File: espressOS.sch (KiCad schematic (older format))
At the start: 22 parts

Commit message: Add temperature sensors
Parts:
- added J?: LMT01_CONN1, symbol Connector_Generic:Conn_01x02
- added J?: LMT01_WIRE1, symbol Connector_Generic:Conn_01x02
- added J?: LMT01_CONN2, symbol Connector_Generic:Conn_01x02
- added J?: LMT01_WIRE2, symbol Connector_Generic:Conn_01x02
- added J?: LMT01_CONN3, symbol Connector_Generic:Conn_01x02
- added J?: LMT01_WIRE3, symbol Connector_Generic:Conn_01x02
- added Q?: 2N3904, Package_TO_SOT_THT:TO-92_Inline, symbol Transistor_BJT:2N3904
- added R?: 10k, symbol Device:R_US
- added U? (x3): LMT01, symbol espressOS:LMT01
- SW?: value SW_Push -> SPST
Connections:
- net labels added: LMT01_1_CTRL, LMT01_2_CTRL, LMT01_3_CTRL, LMT01_OUT
- wire segments 106 -> 130
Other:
- moved on the sheet: C?, R?, SW?, Y?

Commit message: Add LMT01 control pins
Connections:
- wire segments 130 -> 133
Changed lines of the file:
@@
 Text Label 6250 3100 0    50   ~ 0
 SWD_IO
+Wire Wire Line
+	5950 3000 6250 3000
+Text Label 6250 3000 0    50   ~ 0
+LMT01_1_CTRL
+Wire Wire Line
+	5950 4300 6250 4300
+Wire Wire Line
+	5950 4400 6250 4400
+Text Label 6250 4300 0    50   ~ 0
+LMT01_2_CTRL
+Text Label 6250 4400 0    50   ~ 0
+LMT01_3_CTRL
 $EndSCHEMATC

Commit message: Update board
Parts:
- removed J?: FTSH-105-01-L-DV-K, SAMTEC_FTSH-105-01-L-DV-K, symbol FTSH-105-01-L-DV-K:FTSH-105-01-L-DV-K
- added J?: FTSH-105-01-L-DV-K, SAMTEC_FTSH-105-01-L-DV-K, symbol espressOS:FTSH-105-01-L-DV-K
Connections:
- net labels added: AC
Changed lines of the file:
@@
 EESchema Schematic File Version 4
-LIBS:espressOS-cache
 EELAYER 30 0
 EELAYER END
@@
 $EndDescr
 $Comp
-L FTSH-105-01-L-DV-K:FTSH-105-01-L-DV-K J?
-U 1 1 5E4E12B7
-P 5150 6600
-F 0 "J?" H 5150 7070 50  0000 C CNN
-F 1 "FTSH-105-01-L-DV-K" H 5150 6979 50  0000 C CNN
-F 2 "SAMTEC_FTSH-105-01-L-DV-K" H 4950 5750 50  0001 L BNN
-F 3 "FTSH-105-01-L-DV-K-TR" H 4950 5850 50  0001 L BNN
-	1    5150 6600
-	1    0    0    -1
-$EndComp
-$Comp
 L power:VDD #PWR?
 U 1 1 5E4E253E
-P 4300 6350
-F 0 "#PWR?" H 4300 6200 50  0001 C CNN
-F 1 "VDD" H 4317 6523 50  0000 C CNN
-F 2 "" H 4300 6350 50  0001 C CNN
-F 3 "" H 4300 6350 50  0001 C CNN
-	1    4300 6350
-	1    0    0    -1
-$EndComp
-Wire Wire Line
-	4300 6350 4300 6500
-Wire Wire Line
-	4300 6500 4450 6500
+P 5000 6350
+F 0 "#PWR?" H 5000 6200 50  0001 C CNN
+F 1 "VDD" H 5017 6523 50  0000 C CNN
+F 2 "" H 5000 6350 50  0001 C CNN
+F 3 "" H 5000 6350 50  0001 C CNN
+	1    5000 6350
+	1    0    0    -1
+$EndComp
+Wire Wire Line
+	5000 6350 5000 6500
+Wire Wire Line
+	5000 6500 5150 6500
 $Comp
 L power:GND #PWR?
 U 1 1 5E4E2DCF
-P 4300 7150
-F 0 "#PWR?" H 4300 6900 50  0001 C CNN
-F 1 "GND" H 4305 6977 50  0000 C CNN
-F 2 "" H 4300 7150 50  0001 C CNN
-F 3 "" H 4300 7150 50  0001 C CNN
-	1    4300 7150
-	1    0    0    -1
-$EndComp
-Wire Wire Line
-	4300 7150 4300 6900
-Wire Wire Line
-	4300 6600 4450 6600
-Wire Wire Line
-	4450 6700 4300 6700
-Connection ~ 4300 6700
-Wire Wire Line
-	4300 6700 4300 6600
-Wire Wire Line
-	4450 6900 4300 6900
-Connection ~ 4300 6900
-Wire Wire Line
-	4300 6900 4300 6700
+P 5000 7150
+F 0 "#PWR?" H 5000 6900 50  0001 C CNN
+F 1 "GND" H 5005 6977 50  0000 C CNN
+F 2 "" H 5000 7150 50  0001 C CNN
+F 3 "" H 5000 7150 50  0001 C CNN
+	1    5000 7150
+	1    0    0    -1
+$EndComp
+Wire Wire Line
+	5000 7150 5000 6900
+Wire Wire Line
+	5000 6600 5150 6600
+Wire Wire Line
+	5150 6700 5000 6700
+Connection ~ 5000 6700
+Wire Wire Line
+	5000 6700 5000 6600
+Wire Wire Line
+	5150 6900 5000 6900
+Connection ~ 5000 6900
+Wire Wire Line
+	5000 6900 5000 6700
 Wire Wire Line
 	5850 6500 6050 6500
@@
 Text Label 6250 4400 0    50   ~ 0
 LMT01_3_CTRL
+$Comp
+L power:AC #PWR?
+U 1 1 5E40F9F2
+P 1550 1300
+F 0 "#PWR?" H 1550 1200 50  0001 C CNN
+F 1 "AC" H 1550 1575 50  0000 C CNN
+F 2 "" H 1550 1300 50  0001 C CNN
+F 3 "" H 1550 1300 50  0001 C CNN
+	1    1550 1300
+	1    0    0    -1
+$EndComp
+$Comp
+L espressOS:FTSH-105-01-L-DV-K J?
+U 1 1 5E637338
+P 5500 6600
+F 0 "J?" H 5500 6970 50  0000 C CNN
+F 1 "FTSH-105-01-L-DV-K" H 5500 6879 50  0000 C CNN
+F 2 "SAMTEC_FTSH-105-01-L-DV-K" H 5350 5900 50  0001 L BNN
+F 3 "FTSH-105-01-L-DV-K-TR" H 5350 6000 50  0001 L BNN
+	1    5500 6600
+	1    0    0    -1
+$EndComp
 $EndSCHEMATC

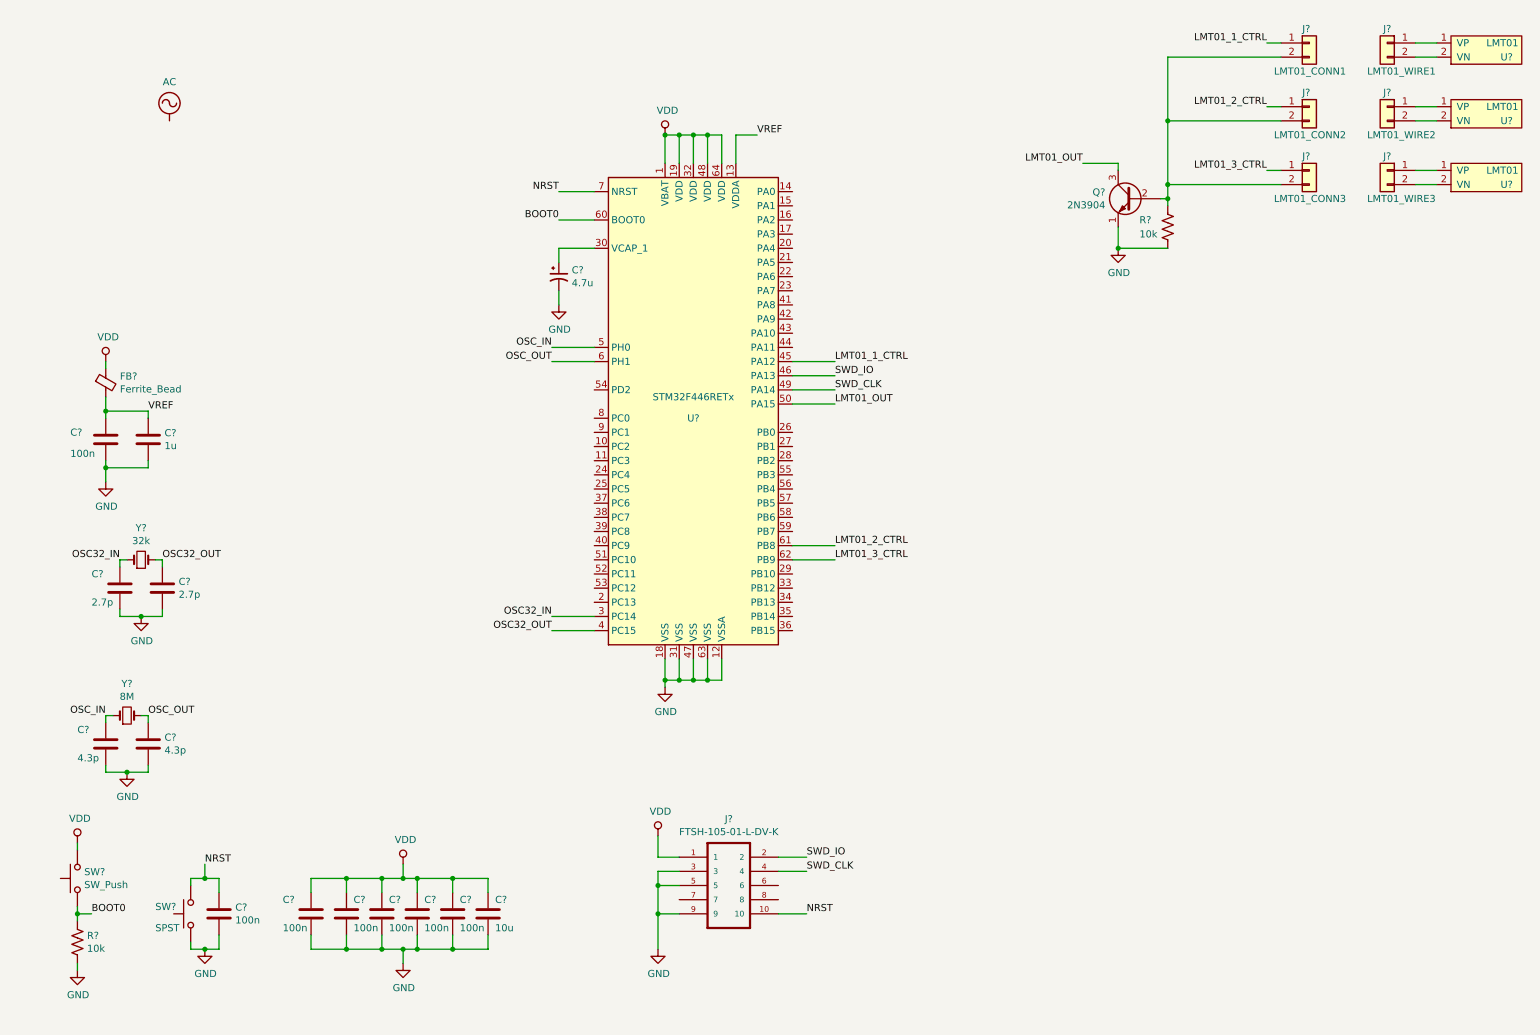
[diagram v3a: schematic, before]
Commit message: Add many components and signals
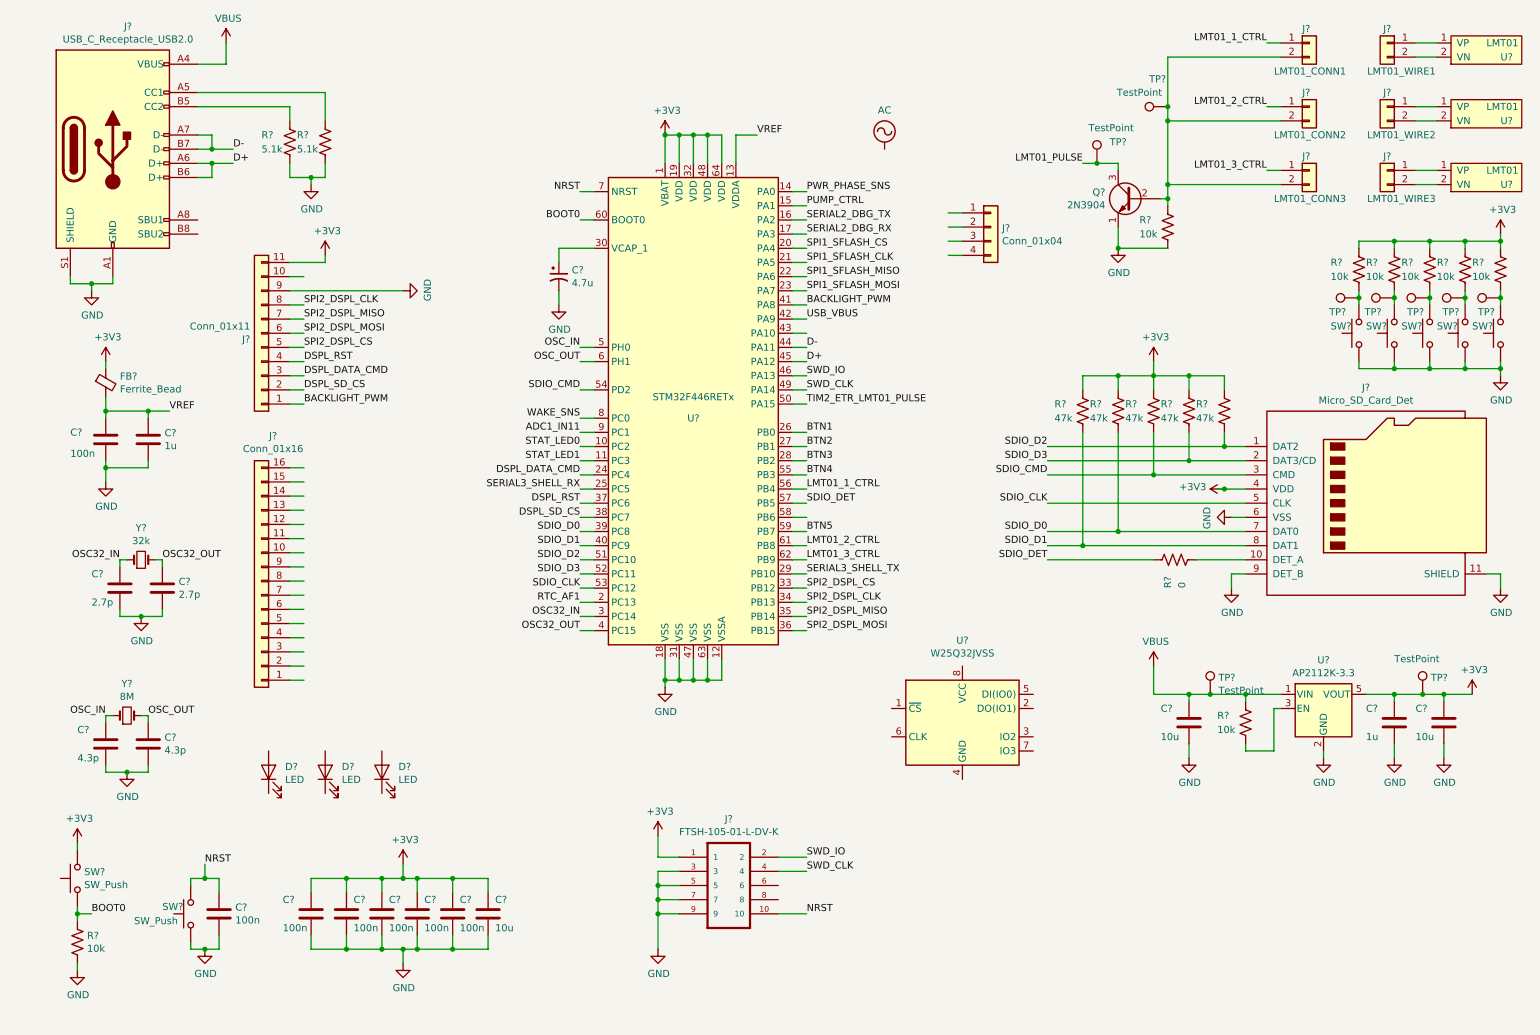
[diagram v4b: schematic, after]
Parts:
- removed SW?: SPST, symbol Switch:SW_Push
- added C?: 1u, symbol Device:C
- added C? (x2): 10u, symbol Device:C
- added D? (x3): LED, symbol Device:LED
- added J?: Micro_SD_Card_Det, symbol Connector:Micro_SD_Card_Det
- added J?: USB_C_Receptacle_USB2.0, symbol Connector:USB_C_Receptacle_USB2.0
- added J?: Conn_01x11, symbol Connector_Generic:Conn_01x11
- added J?: Conn_01x04, symbol Connector_Generic:Conn_01x04
- added J?: Conn_01x16, symbol Connector_Generic:Conn_01x16
- added R? (x2): 5.1k, symbol Device:R_US
- added R? (x5): 47k, symbol Device:R_US
- added R? (x6): 10k, symbol Device:R_US
- added R?: 0, symbol Device:R_US
- added SW? (x6): SW_Push, symbol Switch:SW_Push
- added TP? (x9): TestPoint, symbol Connector:TestPoint
- added U?: W25Q32JVSS, Package_SO:SOIC-8_5.23x5.23mm_P1.27mm, symbol Memory_Flash:W25Q32JVSS
- added U?: AP2112K-3.3, Package_TO_SOT_SMD:SOT-23-5, symbol Regulator_Linear:AP2112K-3.3
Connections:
- net labels added: +3V3, ADC1_IN11, BACKLIGHT_PWM, BTN1, BTN2, BTN3, BTN4, BTN5, D+, D-, DSPL_DATA_CMD, DSPL_RST, DSPL_SD_CS, LMT01_PULSE, PUMP_CTRL, PWR_PHASE_SNS, RTC_AF1, SDIO_CLK, SDIO_CMD, SDIO_D0, SDIO_D1, SDIO_D2, SDIO_D3, SDIO_DET, SERIAL2_DBG_RX, SERIAL2_DBG_TX, SERIAL3_SHELL_RX, SERIAL3_SHELL_TX, SPI1_SFLASH_CLK, SPI1_SFLASH_CS, SPI1_SFLASH_MISO, SPI1_SFLASH_MOSI, SPI2_DSPL_CLK, SPI2_DSPL_CS, SPI2_DSPL_MISO, SPI2_DSPL_MOSI, STAT_LED0, STAT_LED1, TIM2_ETR_LMT01_PULSE, USB_VBUS, VBUS, WAKE_SNS
- net labels removed: LMT01_OUT, VDD
- wire segments 133 -> 320

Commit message: Add lots more wiring
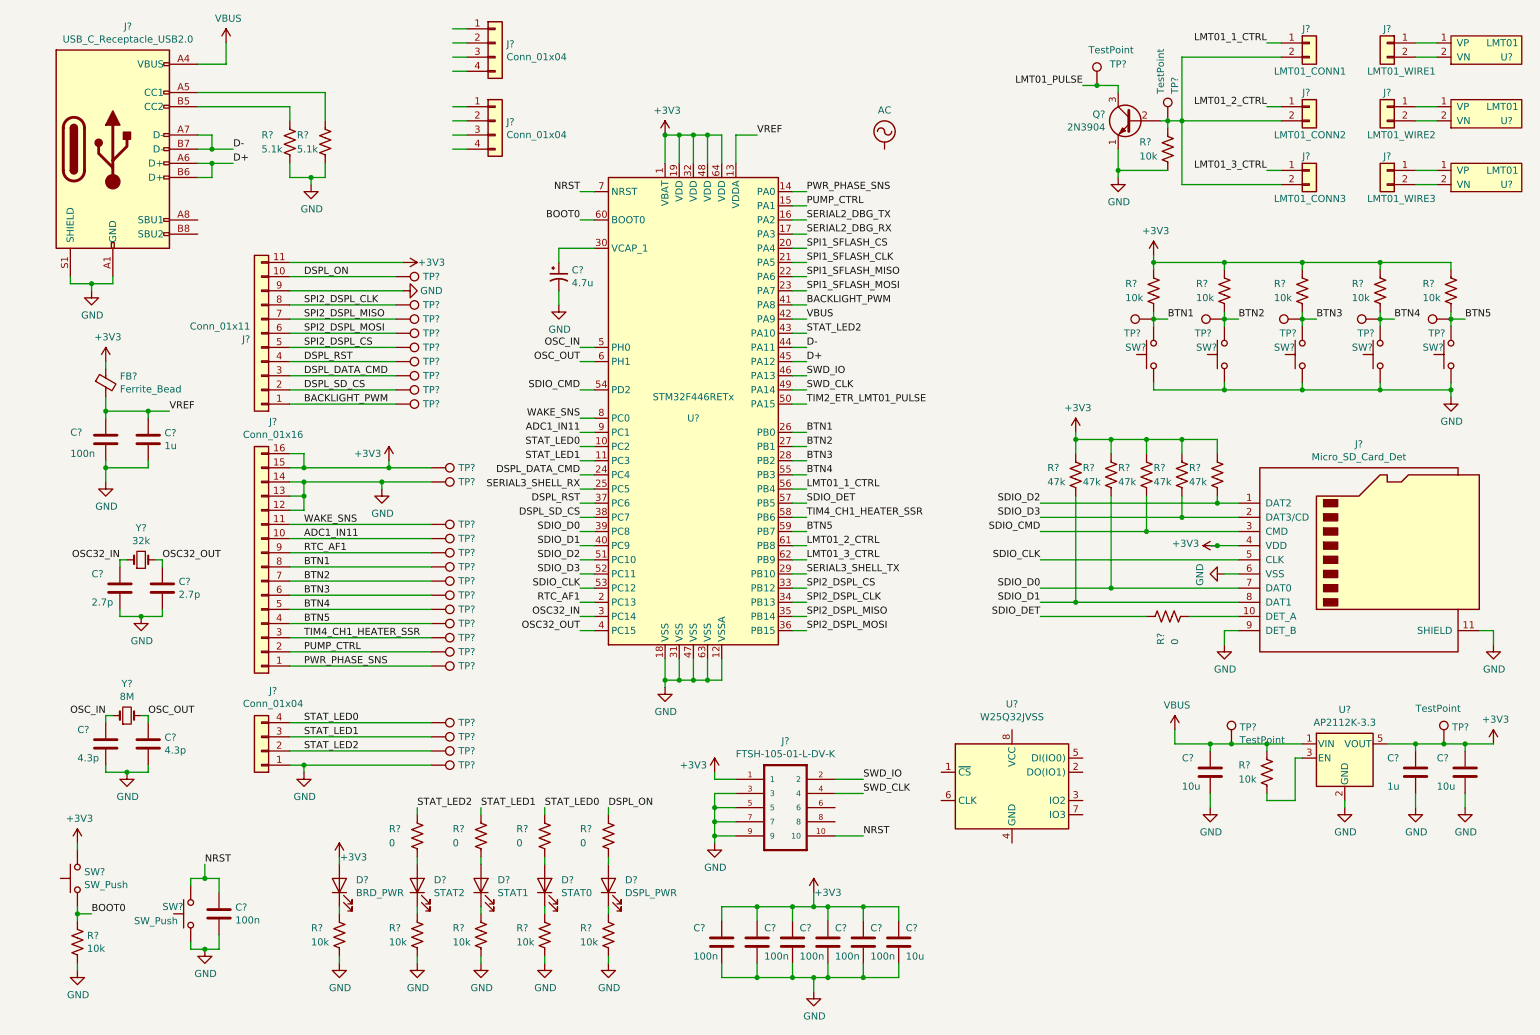
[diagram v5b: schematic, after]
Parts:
- added D?: STAT0, symbol Device:LED
- added D?: DSPL_PWR, symbol Device:LED
- added J? (x2): Conn_01x04, symbol Connector_Generic:Conn_01x04
- added R? (x5): 10k, symbol Device:R_US
- added R? (x4): 0, symbol Device:R_US
- added TP? (x26): TestPoint, symbol Connector:TestPoint
- D?: value LED -> BRD_PWR
- D?: value LED -> STAT2
- D?: value LED -> STAT1
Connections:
- net labels added: DSPL_ON, STAT_LED2, TIM4_CH1_HEATER_SSR
- net labels removed: USB_VBUS
- wire segments 320 -> 362
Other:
- moved on the sheet: C?, D?, J?, Q?, R?, SW?, TP?, U?

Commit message: Add SFLASH
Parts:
- removed U?: W25Q32JVSS, Package_SO:SOIC-8_5.23x5.23mm_P1.27mm, symbol Memory_Flash:W25Q32JVSS
- added R?: 10k, symbol Device:R_US
- added TP? (x14): TestPoint, symbol Connector:TestPoint
- added U?: W25Q16JV, Package_SO:SOIC-8-1EP_3.9x4.9mm_P1.27mm_EP2.29x3mm, symbol espressOS:W25Q16JV
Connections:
- net +3V3: now also J?.1 (Pin_1), J?.1 (Pin_1), R?.1, U?.3 (~WP), U?.7 (~HOLD), U?.8 (VCC)
- net GND: now also J?.4 (Pin_4), J?.4 (Pin_4), U?.4 (VSS)
- net LMT01_1_CTRL: now also TP?.1
- net LMT01_2_CTRL: now also TP?.1
- net LMT01_3_CTRL: now also TP?.1
- net SDIO_CLK: now also TP?.1
- net SDIO_CMD: now also TP?.1
- net SDIO_D0: now also TP?.1
- net SDIO_D1: now also TP?.1
- net SDIO_D2: now also TP?.1
- net SDIO_D3: now also TP?.1
- net SDIO_DET: now also TP?.1
- net SPI1_SFLASH_CLK: now also TP?.1, U?.6 (CLK)
- net SPI1_SFLASH_CS: now also R?.2, TP?.1, U?.1 (~CS)
- net SPI1_SFLASH_MISO: now also TP?.1, U?.2 (DO)
- net SPI1_SFLASH_MOSI: now also TP?.1, U?.5 (DI)
- net TIM4_CH1_HEATER_SSR renamed TIM4_CH1_HEAT_SSR
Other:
- moved on the sheet: C?, FB?, J?, R?, TP?, U?, Y?
